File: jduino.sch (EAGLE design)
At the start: 18 parts, among them IC1 LM2936Z-5.0, IC2 ATMEGA48/88/168-PU, J1 Analog I/O, J2 Digital I/O, J3 Digital I/O, J5 Power Jumpers, J6 FTDI Jumpers, Q1 16 mHz

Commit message: Final fixes for printing.
Replaced power IC with 2931. Added an LED on pin 13.
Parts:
- added LED2: LED 13, led:LED3MM
- added R3: 330, rcl:R-US_0204/5
- IC1: value LM2936Z-5.0 -> L4931; device national-semiconductor:LM2936Z-5.0 -> jb:L4931
- J7: value (none) -> POWER 6 - 36V
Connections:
- removed net D1: IC2.PD1(TXD/PCINT17), J2.2, J6.2
- new net N$4: LED2.C, R3.2
- net +5V: now also IC1.VOUT; no longer IC1.VO
- net D13: now also LED2.A
- net GND: now also R3.1
- net RESET: now also IC2.PD1(TXD/PCINT17), J2.2, J6.2
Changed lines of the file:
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@@
 <part name="SUPPLY16" library="supply2" deviceset="GND" device=""/>
 <part name="D1" library="SparkFun-DiscreteSemi" deviceset="DIODE" device="PTH" value="1N4001"/>
-<part name="IC1" library="national-semiconductor" deviceset="LM2936?*" device="Z" technology="-5.0"/>
 <part name="C2" library="SparkFun-Passives" deviceset="CAP" device="PTH2" value="0.1uF"/>
 <part name="C4" library="SparkFun-Passives" deviceset="CAP" device="PTH2" value="0.1uF"/>
 <part name="FRAME1" library="SparkFun-Aesthetics" deviceset="FRAME-LETTER" device=""/>
-<part name="J7" library="con-jack" deviceset="JACK-PLUG" device="1"/>
+<part name="J7" library="con-jack" deviceset="JACK-PLUG" device="1" value="POWER 6 - 36V"/>
+<part name="IC1" library="jb" deviceset="L4931" device=""/>
+<part name="LED2" library="led" deviceset="LED" device="3MM" value="LED 13"/>
+<part name="R3" library="rcl" deviceset="R-US_" device="0204/5" value="330"/>
+<part name="SUPPLY15" library="supply2" deviceset="GND" device=""/>
 </parts>
 <sheets>
@@
 <instance part="SUPPLY16" gate="GND" x="-15.24" y="-66.04"/>
 <instance part="D1" gate="G$1" x="43.18" y="45.72"/>
-<instance part="IC1" gate="G$1" x="78.74" y="43.18"/>
 <instance part="C2" gate="G$1" x="-101.6" y="-27.94"/>
 <instance part="C4" gate="G$1" x="-68.58" y="43.18" rot="R90"/>
@@
 <instance part="FRAME1" gate="G$2" x="12.7" y="-91.44"/>
 <instance part="J7" gate="G$1" x="20.32" y="40.64"/>
+<instance part="IC1" gate="G$1" x="78.74" y="43.18"/>
+<instance part="LED2" gate="G$1" x="-25.4" y="-50.8"/>
+<instance part="R3" gate="G$1" x="-25.4" y="-66.04" rot="R90"/>
+<instance part="SUPPLY15" gate="GND" x="-25.4" y="-78.74"/>
 </instances>
 <busses>
@@
 </segment>
 <segment>
-<pinref part="IC1" gate="G$1" pin="GND"/>
 <pinref part="SUPPLY2" gate="GND" pin="GND"/>
-<wire x1="78.74" y1="35.56" x2="78.74" y2="27.94" width="0.1524" layer="91"/>
 <wire x1="78.74" y1="27.94" x2="78.74" y2="25.4" width="0.1524" layer="91"/>
 <wire x1="27.94" y1="40.64" x2="27.94" y2="27.94" width="0.1524" layer="91"/>
@@
 <wire x1="25.4" y1="40.64" x2="27.94" y2="40.64" width="0.1524" layer="91"/>
 <junction x="25.4" y="40.64"/>
+<wire x1="78.74" y1="33.02" x2="78.74" y2="27.94" width="0.1524" layer="91"/>
+<pinref part="IC1" gate="G$1" pin="GND"/>
+</segment>
+<segment>
+<pinref part="R3" gate="G$1" pin="1"/>
+<pinref part="SUPPLY15" gate="GND" pin="GND"/>
+<wire x1="-25.4" y1="-71.12" x2="-25.4" y2="-76.2" width="0.1524" layer="91"/>
 </segment>
 </net>
@@
 </segment>
 <segment>
-<wire x1="96.52" y1="40.64" x2="96.52" y2="45.72" width="0.1524" layer="91"/>
 <pinref part="SUPPLY8" gate="+5V" pin="+5V"/>
 <pinref part="C1" gate="G$1" pin="+"/>
-<pinref part="IC1" gate="G$1" pin="VO"/>
+<wire x1="96.52" y1="40.64" x2="96.52" y2="45.72" width="0.1524" layer="91"/>
 <wire x1="96.52" y1="45.72" x2="96.52" y2="53.34" width="0.1524" layer="91"/>
-<wire x1="88.9" y1="45.72" x2="96.52" y2="45.72" width="0.1524" layer="91"/>
+<wire x1="91.44" y1="45.72" x2="96.52" y2="45.72" width="0.1524" layer="91"/>
 <junction x="96.52" y="45.72"/>
+<pinref part="IC1" gate="G$1" pin="VOUT"/>
 </segment>
 <segment>
@@
 <segment>
 <pinref part="J5" gate="G$1" pin="1"/>
-<wire x1="-10.16" y1="50.8" x2="-10.16" y2="71.12" width="0.1524" layer="91"/>
+<wire x1="-10.16" y1="43.18" x2="-10.16" y2="71.12" width="0.1524" layer="91"/>
 <label x="-17.78" y="50.8" size="1.778" layer="95"/>
+<wire x1="-43.18" y1="43.18" x2="-25.4" y2="43.18" width="0.1524" layer="91"/>
+<wire x1="-43.18" y1="43.18" x2="-43.18" y2="71.12" width="0.1524" layer="91"/>
+<pinref part="J6" gate="G$1" pin="2"/>
+<pinref part="IC2" gate="1" pin="PD1(TXD/PCINT17)"/>
+<wire x1="-30.48" y1="-7.62" x2="-25.4" y2="-7.62" width="0.1524" layer="91"/>
+<pinref part="J2" gate="G$1" pin="2"/>
+<label x="-20.32" y="-7.62" size="1.778" layer="95"/>
+<wire x1="-25.4" y1="-7.62" x2="-7.62" y2="-7.62" width="0.1524" layer="91"/>
+<wire x1="-25.4" y1="43.18" x2="-25.4" y2="-7.62" width="0.1524" layer="91"/>
+<junction x="-25.4" y="-7.62"/>
+<wire x1="-10.16" y1="43.18" x2="-25.4" y2="43.18" width="0.1524" layer="91"/>
+<junction x="-25.4" y="43.18"/>
 </segment>
 </net>
@@
 </segment>
 </net>
-<net name="D1" class="0">
-<segment>
-<wire x1="-43.18" y1="43.18" x2="-25.4" y2="43.18" width="0.1524" layer="91"/>
-<wire x1="-43.18" y1="43.18" x2="-43.18" y2="71.12" width="0.1524" layer="91"/>
-<pinref part="J6" gate="G$1" pin="2"/>
-<pinref part="IC2" gate="1" pin="PD1(TXD/PCINT17)"/>
-<wire x1="-30.48" y1="-7.62" x2="-25.4" y2="-7.62" width="0.1524" layer="91"/>
-<pinref part="J2" gate="G$1" pin="2"/>
-<label x="-20.32" y="-7.62" size="1.778" layer="95"/>
-<wire x1="-25.4" y1="-7.62" x2="-7.62" y2="-7.62" width="0.1524" layer="91"/>
-<wire x1="-25.4" y1="43.18" x2="-25.4" y2="-7.62" width="0.1524" layer="91"/>
-<junction x="-25.4" y="-7.62"/>
-</segment>
-</net>
 <net name="D2" class="0">
 <segment>
@@
 <net name="D13" class="0">
 <segment>
-<wire x1="-30.48" y1="-40.64" x2="-7.62" y2="-40.64" width="0.1524" layer="91"/>
+<wire x1="-30.48" y1="-40.64" x2="-25.4" y2="-40.64" width="0.1524" layer="91"/>
 <pinref part="IC2" gate="1" pin="PB5(SCK/PCINT5)"/>
 <pinref part="J3" gate="G$1" pin="6"/>
 <label x="-20.32" y="-40.64" size="1.778" layer="95"/>
+<pinref part="LED2" gate="G$1" pin="A"/>
+<wire x1="-25.4" y1="-40.64" x2="-7.62" y2="-40.64" width="0.1524" layer="91"/>
+<wire x1="-25.4" y1="-48.26" x2="-25.4" y2="-40.64" width="0.1524" layer="91"/>
+<junction x="-25.4" y="-40.64"/>
 </segment>
 </net>
@@
 <segment>
 <pinref part="D1" gate="G$1" pin="C"/>
-<pinref part="IC1" gate="G$1" pin="VIN"/>
 <wire x1="45.72" y1="45.72" x2="58.42" y2="45.72" width="0.1524" layer="91"/>
 <pinref part="C3" gate="G$1" pin="+"/>
-<wire x1="58.42" y1="45.72" x2="68.58" y2="45.72" width="0.1524" layer="91"/>
 <wire x1="58.42" y1="45.72" x2="58.42" y2="40.64" width="0.1524" layer="91"/>
+<wire x1="58.42" y1="45.72" x2="66.04" y2="45.72" width="0.1524" layer="91"/>
 <junction x="58.42" y="45.72"/>
+<pinref part="IC1" gate="G$1" pin="VIN"/>
 </segment>
 </net>
@@
 </segment>
 </net>
+<net name="N$4" class="0">
+<segment>
+<pinref part="LED2" gate="G$1" pin="C"/>
+<pinref part="R3" gate="G$1" pin="2"/>
+<wire x1="-25.4" y1="-55.88" x2="-25.4" y2="-60.96" width="0.1524" layer="91"/>
+</segment>
+</net>

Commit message: Small fixes to the circuit.
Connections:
- new net D1: IC2.PD1(TXD/PCINT17), J2.2, J6.2
- net RESET: no longer IC2.PD1(TXD/PCINT17), J2.2, J6.2

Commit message: Cleaned up area around reset button.
Rotated the reset button. Tied extra button terminals to the live
terminals.
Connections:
- net GND: now also RESET.1
- net RESET: now also RESET.3
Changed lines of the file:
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@@
 <pinref part="RESET" gate="S" pin="2"/>
 <pinref part="SUPPLY4" gate="GND" pin="GND"/>
+<pinref part="RESET" gate="S" pin="1"/>
+<wire x1="-109.22" y1="17.78" x2="-109.22" y2="20.32" width="0.1524" layer="91"/>
+<junction x="-109.22" y="17.78"/>
 </segment>
 <segment>
@@
 <pinref part="C4" gate="G$1" pin="1"/>
 <label x="-96.52" y="15.24" size="1.778" layer="95"/>
+<pinref part="RESET" gate="S" pin="3"/>
+<wire x1="-99.06" y1="17.78" x2="-99.06" y2="20.32" width="0.1524" layer="91"/>
+<junction x="-99.06" y="17.78"/>
 </segment>
 <segment>

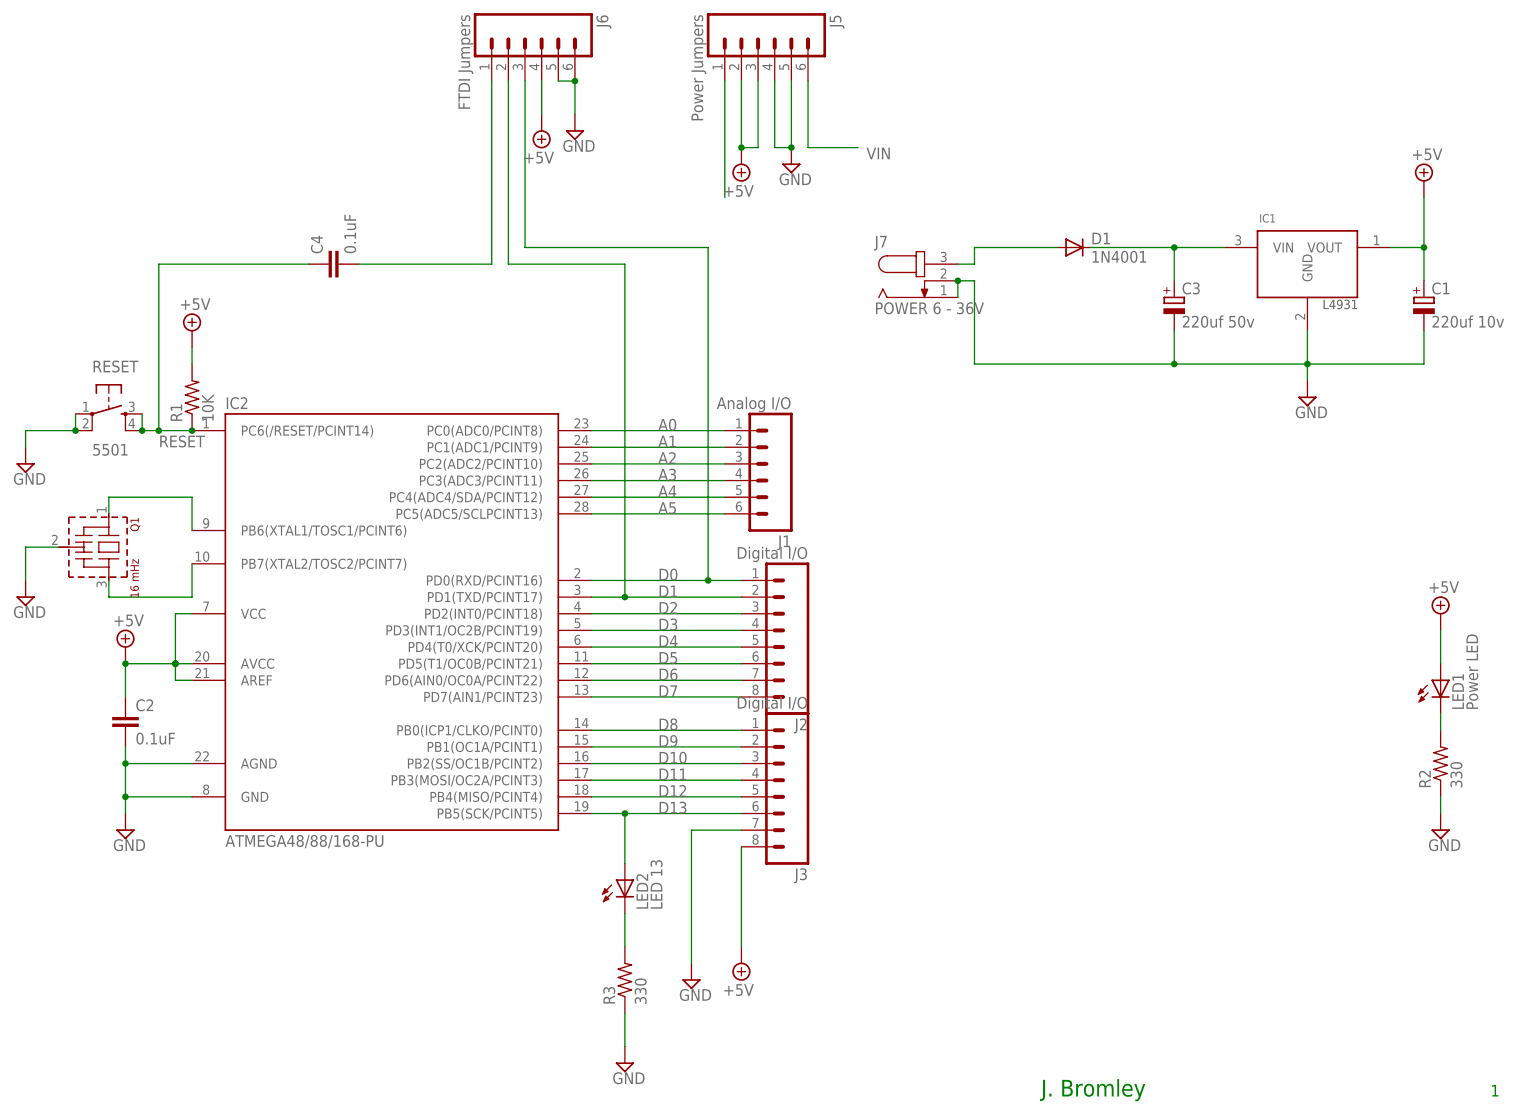
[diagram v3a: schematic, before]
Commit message: Fixed pad sizes.
Replaced original parts from the Arduino robotics book with components
from the SparkFun libraries so that pads would be properly sized.
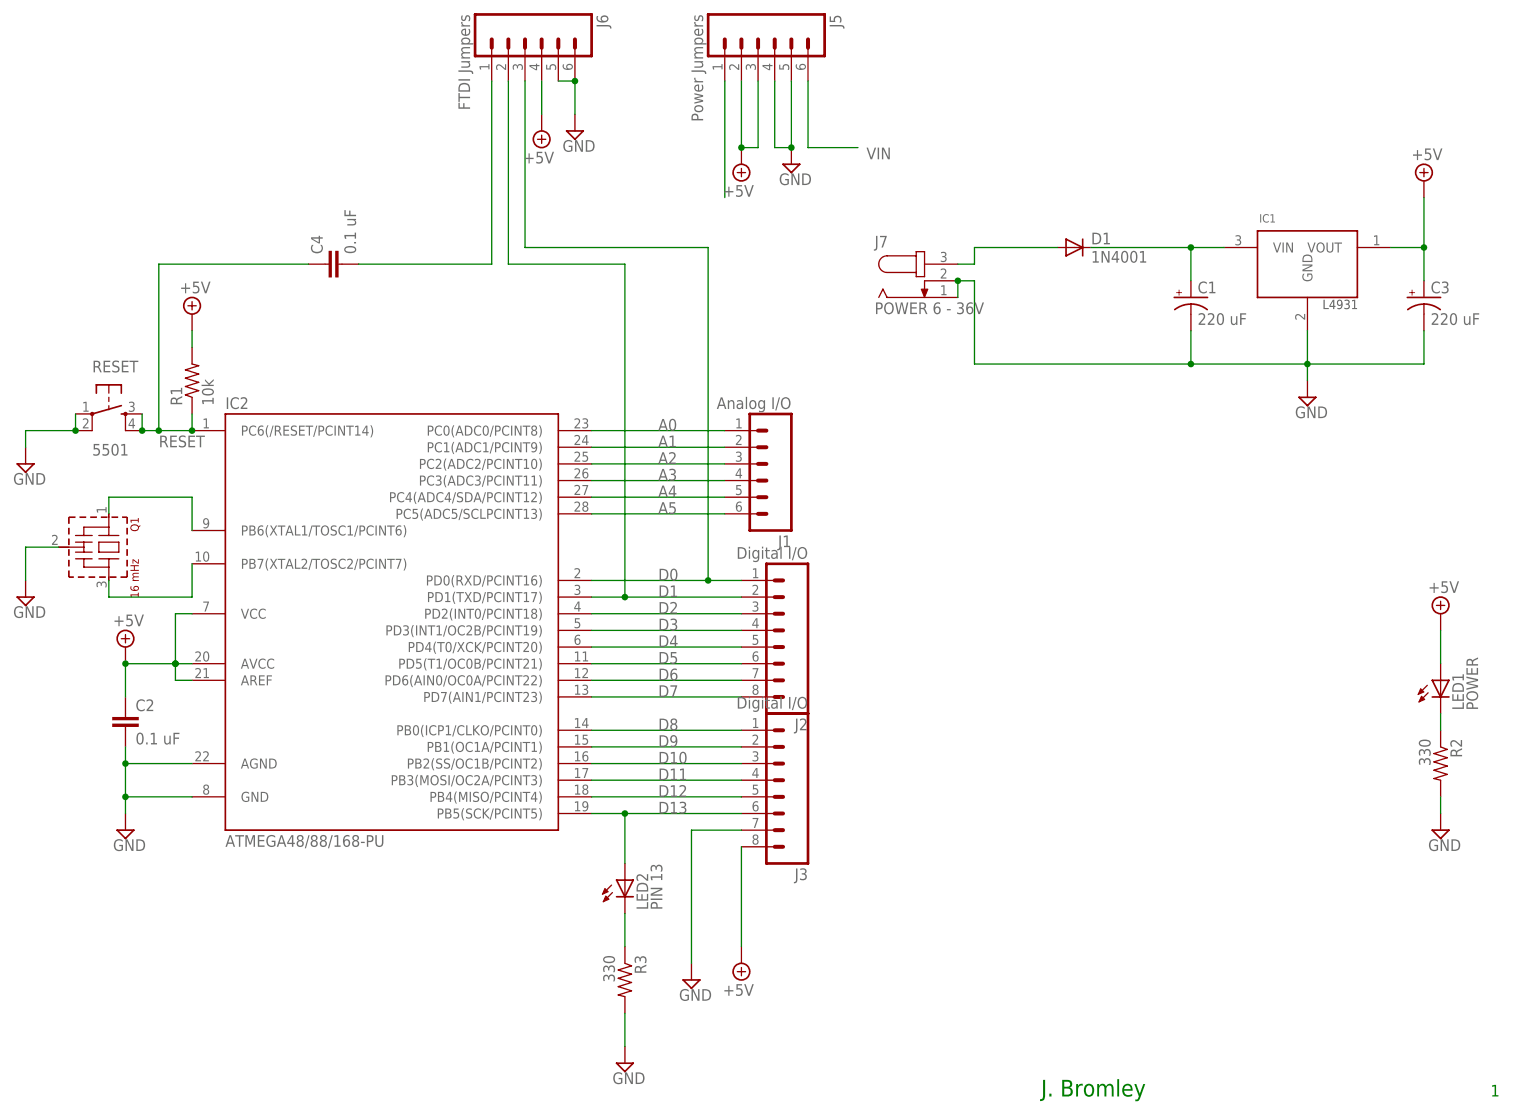
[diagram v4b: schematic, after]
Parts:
- C1: value 220uf 10v -> 220 uF; device rcl:CPOL-EUE2.5-6 -> SparkFun-Capacitors:CAP_POLPTH2
- C2, C4: value 0.1uF -> 0.1 uF; device SparkFun-Passives:CAPPTH2 -> SparkFun-Capacitors:CAPPTH
- C3: value 220uf 50v -> 220 uF; device rcl:CPOL-EUE2.5-6 -> SparkFun-Capacitors:CAP_POLPTH2
- LED1: value Power LED -> POWER; device led:LED3MM -> SparkFun-LED:LED3MM
- LED2: value LED 13 -> PIN 13; device led:LED3MM -> SparkFun-LED:LED3MM
- R1: value 10K -> 10k; device rcl:R-US_0204/5 -> SparkFun-Passives:RESISTORAXIAL-0.3
- R2, R3: device rcl:R-US_0204/5 -> SparkFun-Resistors:RESISTORAXIAL-0.3
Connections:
- net +5V: now also C3.+; no longer C1.+
- net GND: now also R2.2, R3.2; no longer R2.1, R3.1
- net N$26: now also R2.1; no longer R2.2
- net N$4: now also R3.1; no longer R3.2
- net N$6: now also C1.+; no longer C3.+
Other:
- moved on the sheet: C1, C3, R1, R2, R3
